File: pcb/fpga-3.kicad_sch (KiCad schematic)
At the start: 5 parts, among them U5 XC7A35T-FGG484

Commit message: reorg hierarchical, define buses
added bus definitions, aliasing, reorganized sub-sheets for hierarchical interpretation, grouped fpga. pending dram and mram addition
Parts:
- renumbered C5 to C?, C2 to C?, C3 to C?, C4 to C?, U5 to U?
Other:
- moved on the sheet: C?, U?F
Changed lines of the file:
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@@
+	(wire
+		(pts
+			(xy 124.46 107.95) (xy 189.23 107.95)
+		)
+		(stroke
+			(width 0)
+			(type default)
+		)
+	)
 	(wire
 		(pts
@@
 	(wire
 		(pts
-			(xy 162.56 76.2) (xy 193.04 76.2)
+			(xy 124.46 82.55) (xy 154.94 82.55)
 		)
 		(stroke
@@
 	(wire
 		(pts
-			(xy 200.66 53.34) (xy 227.33 53.34)
+			(xy 162.56 59.69) (xy 189.23 59.69)
 		)
 		(stroke
@@
 	(wire
 		(pts
-			(xy 162.56 53.34) (xy 193.04 53.34)
+			(xy 124.46 59.69) (xy 154.94 59.69)
 		)
 		(stroke
@@
 	(wire
 		(pts
-			(xy 162.56 78.74) (xy 179.07 78.74)
+			(xy 124.46 105.41) (xy 189.23 105.41)
 		)
 		(stroke
@@
 	(wire
 		(pts
-			(xy 200.66 76.2) (xy 227.33 76.2)
+			(xy 124.46 85.09) (xy 140.97 85.09)
 		)
 		(stroke
@@
 	(wire
 		(pts
-			(xy 162.56 99.06) (xy 189.23 99.06)
+			(xy 162.56 82.55) (xy 189.23 82.55)
 		)
 		(stroke
@@
 	(wire
 		(pts
-			(xy 162.56 101.6) (xy 189.23 101.6)
+			(xy 139.7 139.7) (xy 166.37 139.7)
 		)
 		(stroke
@@
 	(wire
 		(pts
-			(xy 139.7 139.7) (xy 166.37 139.7)
+			(xy 139.7 147.32) (xy 166.37 147.32)
 		)
 		(stroke
@@
 	(wire
 		(pts
-			(xy 139.7 147.32) (xy 166.37 147.32)
+			(xy 148.59 62.23) (xy 189.23 62.23)
 		)
 		(stroke
@@
 	(wire
 		(pts
-			(xy 186.69 55.88) (xy 227.33 55.88)
+			(xy 148.59 85.09) (xy 189.23 85.09)
 		)
 		(stroke
@@
 	(wire
 		(pts
-			(xy 186.69 78.74) (xy 227.33 78.74)
+			(xy 139.7 144.78) (xy 166.37 144.78)
 		)
 		(stroke
@@
 	(wire
 		(pts
-			(xy 139.7 144.78) (xy 166.37 144.78)
+			(xy 124.46 62.23) (xy 140.97 62.23)
 		)
 		(stroke
@@
 		)
 	)
-	(wire
-		(pts
-			(xy 162.56 55.88) (xy 179.07 55.88)
-		)
-		(stroke
-			(width 0)
-			(type default)
-		)
-	)
 	(label "PCIE_RST_B"
 		(at 158.75 147.32 180)
@@
 	)
 	(label "PCIE_CLK_P"
-		(at 181.61 99.06 180)
+		(at 182.88 105.41 180)
 		(effects
 			(font
@@
 	)
 	(label "PCIE_RX_N"
-		(at 219.71 78.74 180)
+		(at 181.61 85.09 180)
 		(effects
 			(font
@@
 	)
 	(label "PCIE_TX_P"
-		(at 219.71 53.34 180)
+		(at 181.61 59.69 180)
 		(effects
 			(font
@@
 	)
 	(label "PCIE_RX_P"
-		(at 219.71 76.2 180)
+		(at 181.61 82.55 180)
 		(effects
 			(font
@@
 	)
 	(label "PCIE_TX_N"
-		(at 219.71 55.88 180)
+		(at 181.61 62.23 180)
 		(effects
 			(font
@@
 	)
 	(label "PCIE_CLK_N"
-		(at 181.61 101.6 180)
+		(at 182.88 107.95 180)
 		(effects
 			(font
@@
 	(hierarchical_label "PCIE_CLK_N"
 		(shape bidirectional)
-		(at 189.23 101.6 0)
+		(at 189.23 107.95 0)
 		(effects
 			(font
@@
 	(hierarchical_label "PCIE_TX_N"
 		(shape input)
-		(at 227.33 55.88 0)
+		(at 189.23 62.23 0)
 		(effects
 			(font
@@
 	(hierarchical_label "PCIE_RX_N"
 		(shape output)
-		(at 227.33 78.74 0)
+		(at 189.23 85.09 0)
 		(effects
 			(font
@@
 	(hierarchical_label "PCIE_RX_P"
 		(shape output)
-		(at 227.33 76.2 0)
+		(at 189.23 82.55 0)
 		(effects
 			(font
@@
 	(hierarchical_label "PCIE_TX_P"
 		(shape input)
-		(at 227.33 53.34 0)
+		(at 189.23 59.69 0)
 		(effects
 			(font
@@
 	(hierarchical_label "PCIE_CLK_P"
 		(shape bidirectional)
-		(at 189.23 99.06 0)
+		(at 189.23 105.41 0)
 		(effects
 			(font
@@
 	(symbol
 		(lib_id "Device:C")
-		(at 182.88 55.88 90)
+		(at 144.78 62.23 90)
 		(unit 1)
 		(exclude_from_sim no)
@@
 		(on_board yes)
 		(dnp no)
-		(property "Reference" "C5"
-			(at 179.07 54.61 90)
+		(property "Reference" "C?"
+			(at 140.97 60.96 90)
 			(effects
 				(font
@@
 		)
 		(property "Value" "0.1uF"
-			(at 187.96 54.61 90)
+			(at 149.86 60.96 90)
 			(effects
 				(font
@@
 		)
 		(property "Footprint" "Capacitor_SMD:C_0402_1005Metric"
-			(at 186.69 54.9148 0)
+			(at 148.59 61.2648 0)
 			(effects
 				(font
@@
 		)
 		(property "Datasheet" "~"
-			(at 182.88 55.88 0)
+			(at 144.78 62.23 0)
 			(effects
 				(font
@@
 		)
 		(property "Description" "Unpolarized capacitor"
-			(at 182.88 55.88 0)
+			(at 144.78 62.23 0)
 			(effects
 				(font
@@
 		(instances
 			(project "RPi-HwAB-1"
-				(path "/e63e39d7-6ac0-4ffd-8aa3-1841a4541b55/20a31476-4eec-4a3e-82d2-9314270dc40b"
-					(reference "C5")
+				(path "/e63e39d7-6ac0-4ffd-8aa3-1841a4541b55/59d21473-a004-4514-8090-fd93db818925/143e814b-c088-43b0-8f2f-ada8c438e494"
+					(reference "C?")
 					(unit 1)
 				)
@@
 	(symbol
 		(lib_id "FPGA_Xilinx_Artix7:XC7A35T-FGG484")
-		(at 143.51 80.01 0)
+		(at 105.41 86.36 0)
 		(unit 6)
 		(exclude_from_sim no)
@@
 		(dnp no)
 		(fields_autoplaced yes)
-		(property "Reference" "U5"
-			(at 143.51 46.99 0)
+		(property "Reference" "U?"
+			(at 105.41 53.34 0)
 			(effects
 				(font
@@
 		)
 		(property "Value" "XC7A35T-FGG484"
-			(at 143.51 49.53 0)
+			(at 105.41 55.88 0)
 			(effects
 				(font
@@
 		)
 		(property "Footprint" "Package_BGA:Xilinx_FGG484"
-			(at 143.51 80.01 0)
+			(at 105.41 86.36 0)
 			(effects
 				(font
@@
 		)
 		(property "Datasheet" ""
-			(at 143.51 80.01 0)
+			(at 105.41 86.36 0)
 			(effects
 				(font
@@
 		)
 		(property "Description" "Artix 7 T 35 XC7A35T-FGG484"
-			(at 116.84 63.5 0)
+			(at 78.74 69.85 0)
 			(effects
 				(font
@@
 		(instances
 			(project "RPi-HwAB-1"
-				(path "/e63e39d7-6ac0-4ffd-8aa3-1841a4541b55/20a31476-4eec-4a3e-82d2-9314270dc40b"
-					(reference "U5")
+				(path "/e63e39d7-6ac0-4ffd-8aa3-1841a4541b55/59d21473-a004-4514-8090-fd93db818925/143e814b-c088-43b0-8f2f-ada8c438e494"
+					(reference "U?")
 					(unit 6)
 				)
@@
 	(symbol
 		(lib_id "Device:C")
-		(at 196.85 76.2 90)
+		(at 158.75 82.55 90)
 		(unit 1)
 		(exclude_from_sim no)
@@
 		(on_board yes)
 		(dnp no)
-		(property "Reference" "C2"
-			(at 193.04 74.93 90)
+		(property "Reference" "C?"
+			(at 154.94 81.28 90)
 			(effects
 				(font
@@
 		)
 		(property "Value" "0.1uF"
-			(at 201.93 74.93 90)
+			(at 163.83 81.28 90)
 			(effects
 				(font
@@
 		)
 		(property "Footprint" "Capacitor_SMD:C_0402_1005Metric"
-			(at 200.66 75.2348 0)
+			(at 162.56 81.5848 0)
 			(effects
 				(font
@@
 		)
 		(property "Datasheet" "~"
-			(at 196.85 76.2 0)
+			(at 158.75 82.55 0)
 			(effects
 				(font
@@
 		)
 		(property "Description" "Unpolarized capacitor"
-			(at 196.85 76.2 0)
+			(at 158.75 82.55 0)
 			(effects
 				(font
@@
 		)
 		(instances
-			(project ""
-				(path "/e63e39d7-6ac0-4ffd-8aa3-1841a4541b55/20a31476-4eec-4a3e-82d2-9314270dc40b"
-					(reference "C2")
+			(project "RPi-HwAB-1"
+				(path "/e63e39d7-6ac0-4ffd-8aa3-1841a4541b55/59d21473-a004-4514-8090-fd93db818925/143e814b-c088-43b0-8f2f-ada8c438e494"
+					(reference "C?")
 					(unit 1)
 				)
@@
 	(symbol
 		(lib_id "Device:C")
-		(at 182.88 78.74 90)
+		(at 144.78 85.09 90)
 		(unit 1)
 		(exclude_from_sim no)
@@
 		(on_board yes)
 		(dnp no)
-		(property "Reference" "C3"
-			(at 179.07 77.47 90)
+		(property "Reference" "C?"
+			(at 140.97 83.82 90)
 			(effects
 				(font
@@
 		)
 		(property "Value" "0.1uF"
-			(at 187.96 77.47 90)
+			(at 149.86 83.82 90)
 			(effects
 				(font
@@
 		)
 		(property "Footprint" "Capacitor_SMD:C_0402_1005Metric"
-			(at 186.69 77.7748 0)
+			(at 148.59 84.1248 0)
 			(effects
 				(font
@@
 		)
 		(property "Datasheet" "~"
-			(at 182.88 78.74 0)
+			(at 144.78 85.09 0)
 			(effects
 				(font
@@
 		)
 		(property "Description" "Unpolarized capacitor"
-			(at 182.88 78.74 0)
+			(at 144.78 85.09 0)
 			(effects
 				(font
@@
 		(instances
 			(project "RPi-HwAB-1"
-				(path "/e63e39d7-6ac0-4ffd-8aa3-1841a4541b55/20a31476-4eec-4a3e-82d2-9314270dc40b"
-					(reference "C3")
+				(path "/e63e39d7-6ac0-4ffd-8aa3-1841a4541b55/59d21473-a004-4514-8090-fd93db818925/143e814b-c088-43b0-8f2f-ada8c438e494"
+					(reference "C?")
 					(unit 1)
 				)
@@
 	(symbol
 		(lib_id "Device:C")
-		(at 196.85 53.34 90)
+		(at 158.75 59.69 90)
 		(unit 1)
 		(exclude_from_sim no)
@@
 		(on_board yes)
 		(dnp no)
-		(property "Reference" "C4"
-			(at 193.04 52.07 90)
+		(property "Reference" "C?"
+			(at 154.94 58.42 90)
 			(effects
 				(font
@@
 		)
 		(property "Value" "0.1uF"
-			(at 201.93 52.07 90)
+			(at 163.83 58.42 90)
 			(effects
 				(font
@@
 		)
 		(property "Footprint" "Capacitor_SMD:C_0402_1005Metric"
-			(at 200.66 52.3748 0)
+			(at 162.56 58.7248 0)
 			(effects
 				(font
@@
 		)
 		(property "Datasheet" "~"
-			(at 196.85 53.34 0)
+			(at 158.75 59.69 0)
 			(effects
 				(font
@@
 		)
 		(property "Description" "Unpolarized capacitor"
-			(at 196.85 53.34 0)
+			(at 158.75 59.69 0)
 			(effects
 				(font
@@
 		(instances
 			(project "RPi-HwAB-1"
-				(path "/e63e39d7-6ac0-4ffd-8aa3-1841a4541b55/20a31476-4eec-4a3e-82d2-9314270dc40b"
-					(reference "C4")
+				(path "/e63e39d7-6ac0-4ffd-8aa3-1841a4541b55/59d21473-a004-4514-8090-fd93db818925/143e814b-c088-43b0-8f2f-ada8c438e494"
+					(reference "C?")
 					(unit 1)
 				)

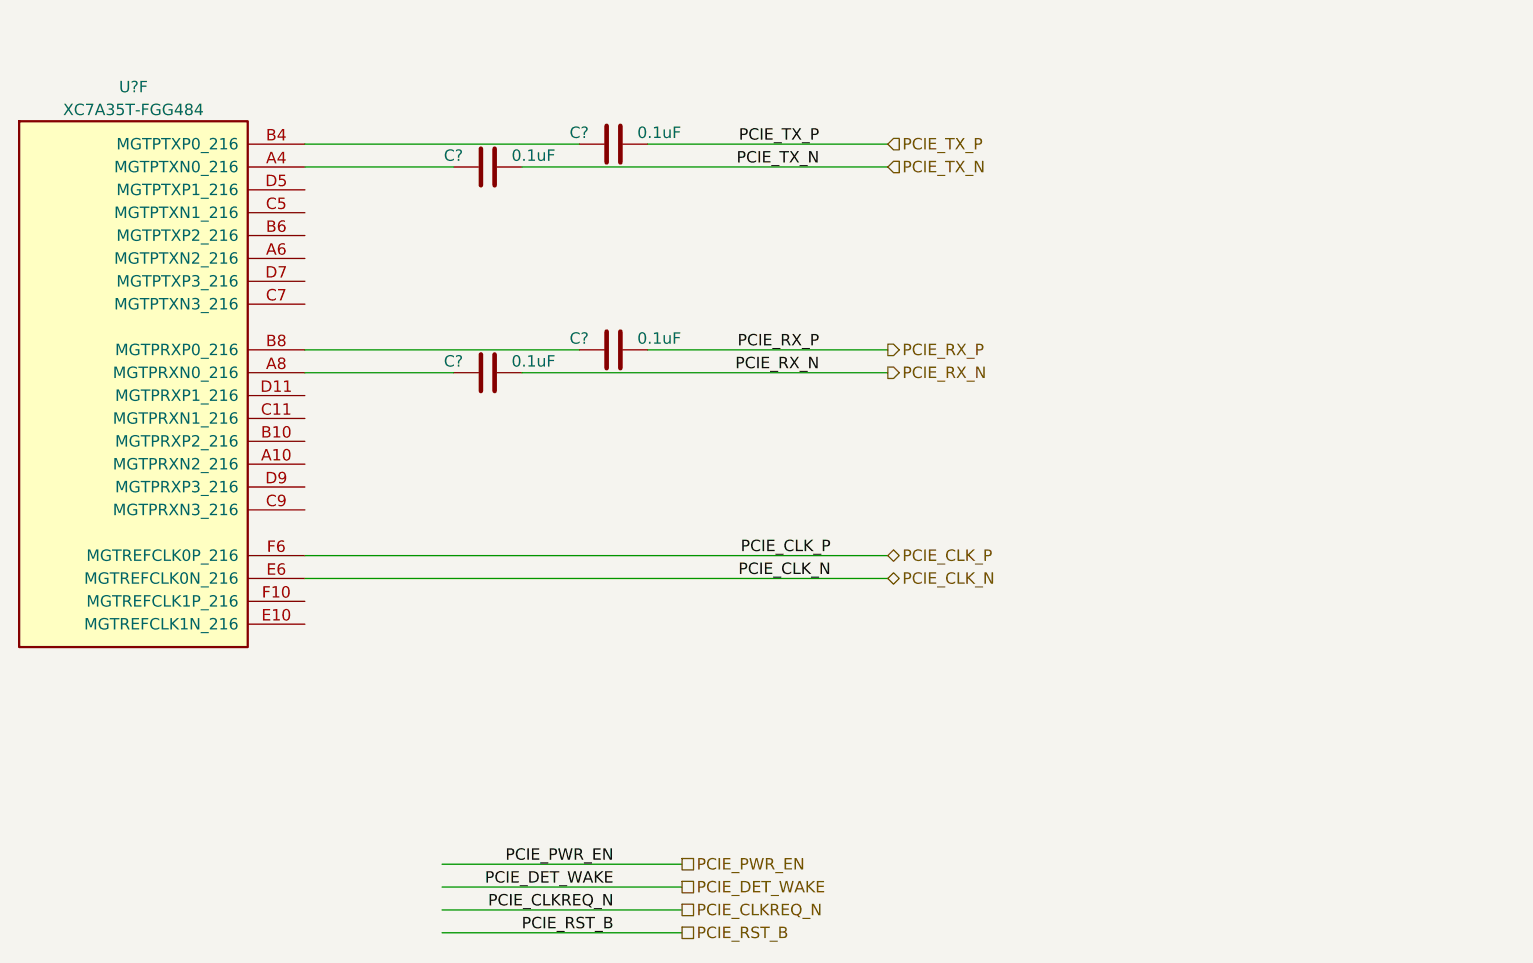
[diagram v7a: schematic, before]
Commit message: completed bus aliasing definitions
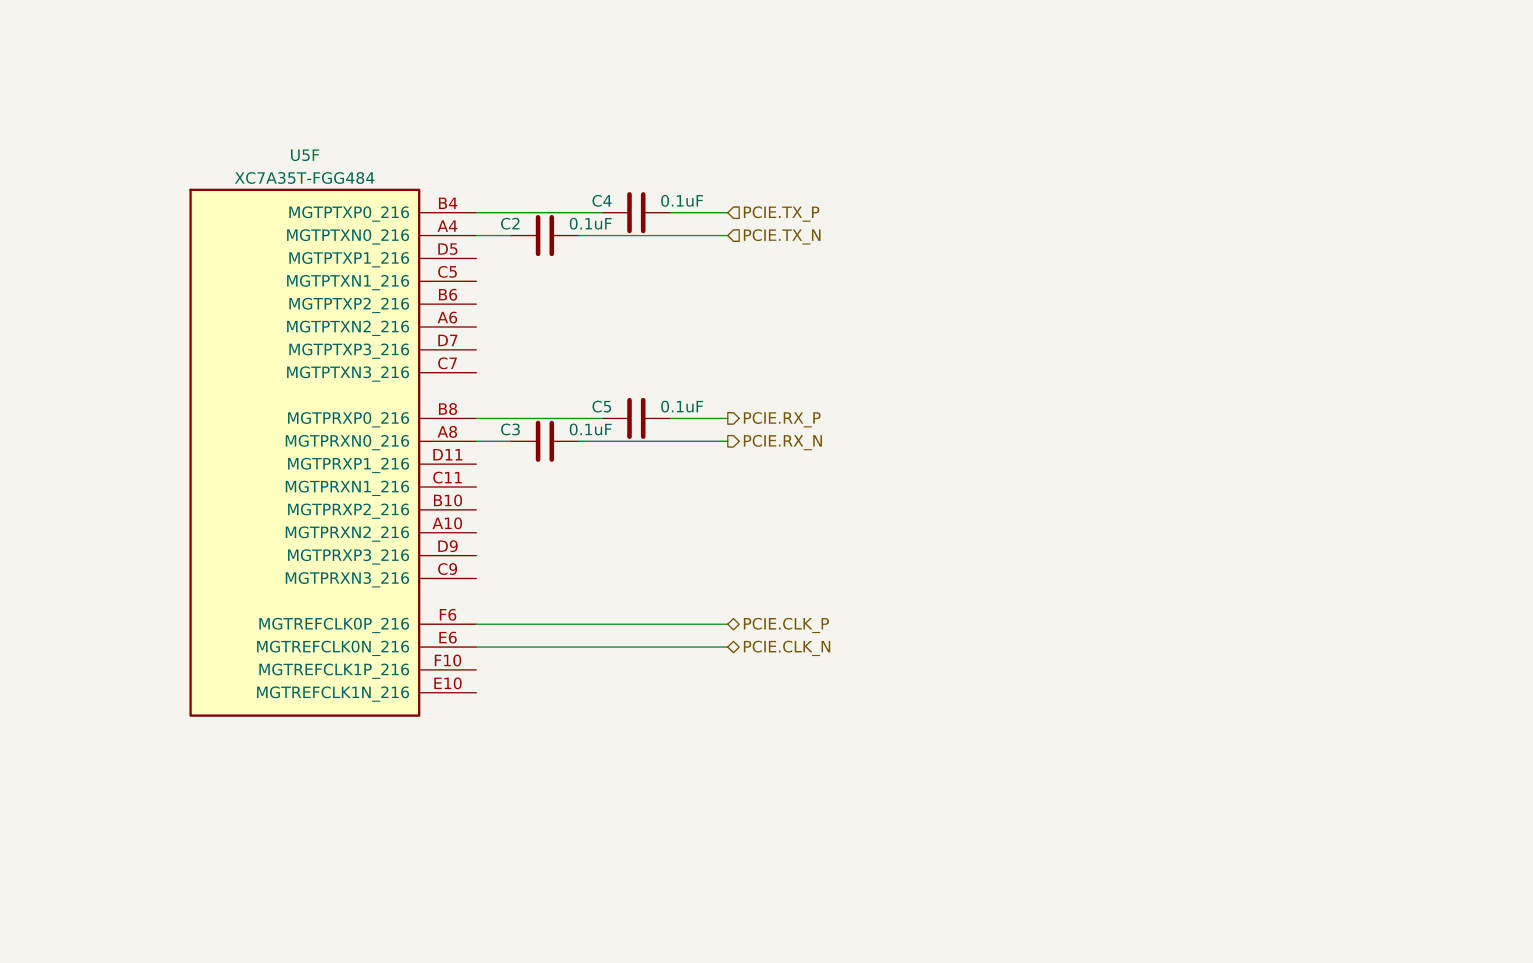
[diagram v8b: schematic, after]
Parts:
- gave numbers to parts that had none: 5
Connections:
- net PCIE_CLK_N renamed PCIE.CLK_N
- net PCIE_CLK_P renamed PCIE.CLK_P
- net PCIE_RX_N renamed PCIE.RX_N
- net PCIE_RX_P renamed PCIE.RX_P
- net PCIE_TX_N renamed PCIE.TX_N
- net PCIE_TX_P renamed PCIE.TX_P
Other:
- moved on the sheet: C2, C3, C4, C5, U5F
